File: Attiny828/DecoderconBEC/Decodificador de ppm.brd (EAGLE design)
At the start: 13.8 x 32.4 mm, 21 parts, among them U1 ATTINY828-AURTQFP32_9X9_MCH-M, U2 AP63205WU-7SOIC_05WU-7_DIO-M

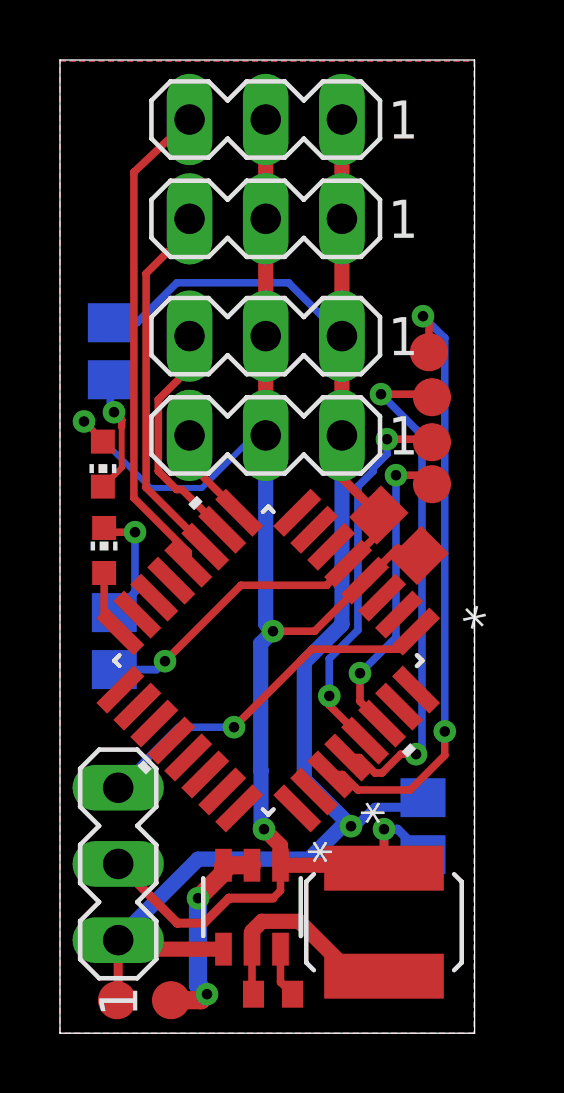
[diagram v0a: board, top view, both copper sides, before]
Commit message: Add files via upload
Se agrego capcitor de entrada del regulador un canal menos y mejor perfil
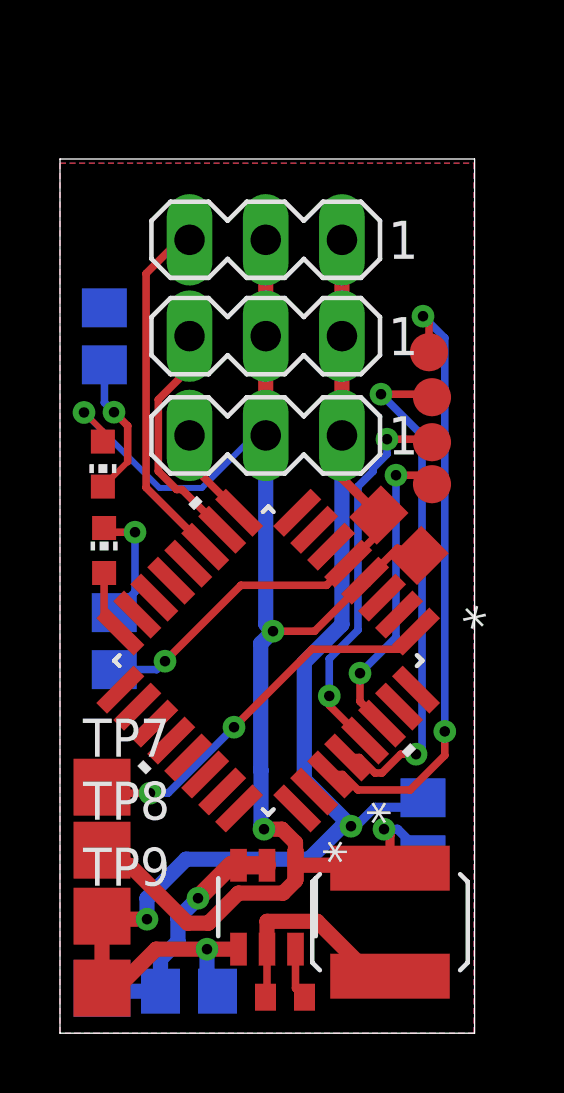
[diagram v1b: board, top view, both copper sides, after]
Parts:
- removed SV1, SV5: (no value), con-lstb:MA03-1
- added C3: (no value), rcl:C0805
- added TP7, TP8, TP9: TPTP19SQ, testpad:TP19SQ
- TP5, TP6: value TPB1,27 -> TPTP19SQ; device testpad:B1,27 -> testpad:TP19SQ
- moved TP5 2.33 mm to (1.40, 1.50), flipped to the bottom
- moved SV4 0.70 mm to (6.86, 26.4)
- moved TP6 0.64 mm to (1.40, 1.50)
- moved R2 0.54 mm to (1.48, 23.2)
- moved U2 0.50 mm to (6.90, 4.20)
- moved BOOT 0.41 mm to (7.50, 1.20)
- moved U$2 0.20 mm to (11.0, 3.70)
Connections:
- removed net N$10: SV5.3, U1.12
- net +5V: now also TP8.TP; no longer SV1.2, SV5.2
- net GND: now also C3.1, TP9.TP; no longer SV1.1, SV5.1
- net N$3: now also TP7.TP; no longer SV1.3
- net V+: now also C3.2
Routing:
- net N$10: track 16.4 -> 0.00 mm
- net GND: track 66.1 -> 57.5 mm, vias 2 -> 4
- net +5V: track 55.0 -> 52.8 mm
- net V+: track 7.01 -> 8.36 mm, vias 2 -> 1
- net N$2: track 3.98 -> 4.72 mm
- net N$3: track 12.1 -> 12.8 mm, vias 1 -> 2
- net N$9: track 12.3 -> 11.8 mm
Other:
- board size 13.8 x 32.4 mm -> 13.8 x 29.1 mm
- board text added: "Por Sol"
- board text removed: "Por Dzohl"
